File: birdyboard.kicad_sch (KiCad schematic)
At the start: 5 parts, among them U3 TMC2208_SILENTSTEPSTICK, U5 Pico

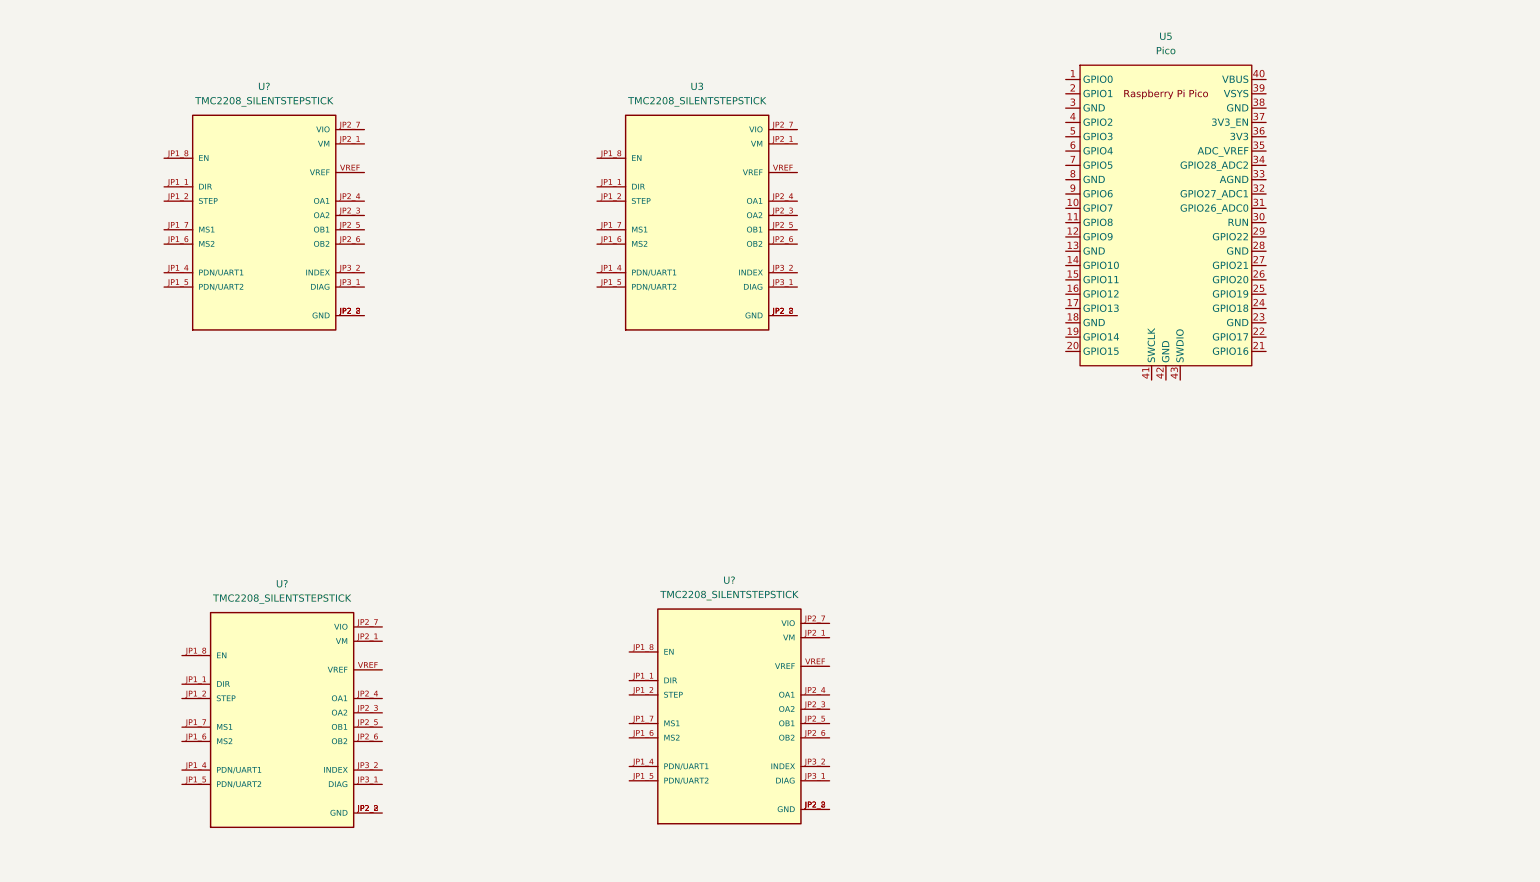
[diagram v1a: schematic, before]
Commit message: Adds the main POWER terminals, adds a symbol and net names for AS5047 board header
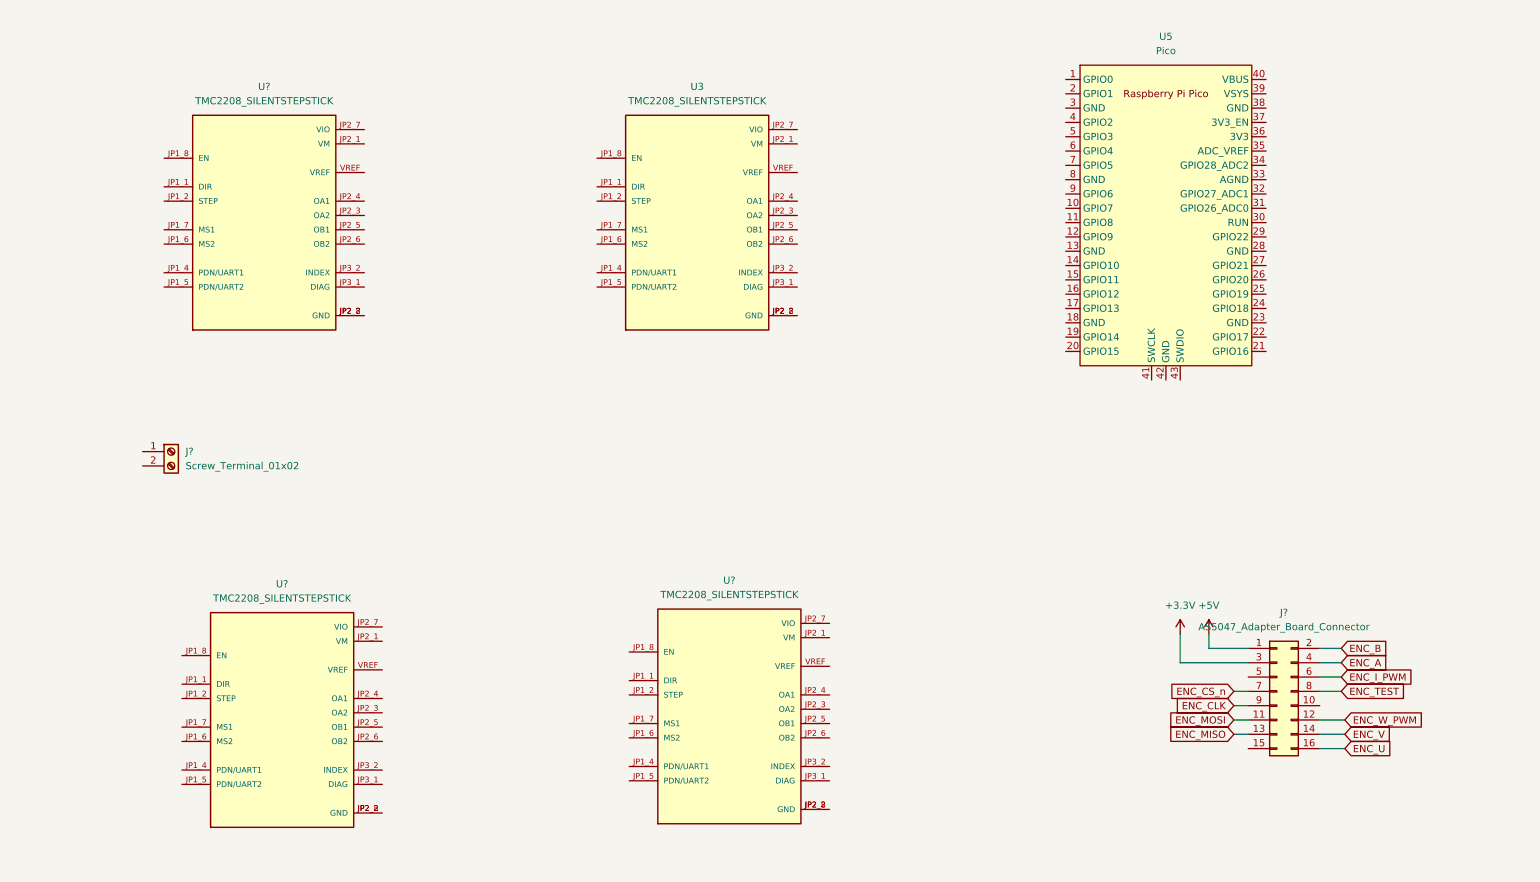
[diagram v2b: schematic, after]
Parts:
- added J?: Screw_Terminal_01x02, birdyboard:CUI_TBP01R2-508-02BE, symbol Connector:Screw_Terminal_01x02
- added J?: AS5047_Adapter_Board_Connector, symbol Connector_Generic:Conn_02x08_Odd_Even
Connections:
- new net +3V3: J?.3 (Pin_3)
- new net +5V: J?.1 (Pin_1)
- new net ENC_A: J?.4 (Pin_4)
- new net ENC_B: J?.2 (Pin_2)
- new net ENC_CLK: J?.9 (Pin_9)
- new net ENC_CS_n: J?.7 (Pin_7)
- new net ENC_I_PWM: J?.6 (Pin_6)
- new net ENC_MISO: J?.13 (Pin_13)
- new net ENC_MOSI: J?.11 (Pin_11)
- new net ENC_TEST: J?.8 (Pin_8)
- new net ENC_U: J?.16 (Pin_16)
- new net ENC_V: J?.14 (Pin_14)
- new net ENC_W_PWM: J?.12 (Pin_12)
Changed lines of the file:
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@@
 (kicad_sch (version 20211123) (generator eeschema)
   (paper "A4")
+  (wire (pts (xy 249.555 140.97) (xy 253.365 140.97))
+    (stroke (width 0) (type default) (color 0 0 0 0))
+  )
+  (wire (pts (xy 249.555 153.67) (xy 254 153.67))
+    (stroke (width 0) (type default) (color 0 0 0 0))
+  )
+  (wire (pts (xy 249.555 148.59) (xy 254 148.59))
+    (stroke (width 0) (type default) (color 0 0 0 0))
+  )
+  (wire (pts (xy 234.315 146.05) (xy 236.855 146.05))
+    (stroke (width 0) (type default) (color 0 0 0 0))
+  )
+  (wire (pts (xy 249.555 151.13) (xy 254 151.13))
+    (stroke (width 0) (type default) (color 0 0 0 0))
+  )
+  (wire (pts (xy 249.555 143.51) (xy 253.365 143.51))
+    (stroke (width 0) (type default) (color 0 0 0 0))
+  )
+  (wire (pts (xy 249.555 138.43) (xy 253.365 138.43))
+    (stroke (width 0) (type default) (color 0 0 0 0))
+  )
+  (wire (pts (xy 236.855 135.89) (xy 229.87 135.89))
+    (stroke (width 0) (type default) (color 0 0 0 0))
+  )
+  (wire (pts (xy 249.555 135.89) (xy 253.365 135.89))
+    (stroke (width 0) (type default) (color 0 0 0 0))
+  )
+  (wire (pts (xy 234.315 143.51) (xy 236.855 143.51))
+    (stroke (width 0) (type default) (color 0 0 0 0))
+  )
+  (wire (pts (xy 224.79 138.43) (xy 224.79 133.35))
+    (stroke (width 0) (type default) (color 0 0 0 0))
+  )
+  (wire (pts (xy 229.87 135.89) (xy 229.87 133.35))
+    (stroke (width 0) (type default) (color 0 0 0 0))
+  )
+  (wire (pts (xy 234.315 148.59) (xy 236.855 148.59))
+    (stroke (width 0) (type default) (color 0 0 0 0))
+  )
+  (wire (pts (xy 234.315 151.13) (xy 236.855 151.13))
+    (stroke (width 0) (type default) (color 0 0 0 0))
+  )
+  (wire (pts (xy 236.855 138.43) (xy 224.79 138.43))
+    (stroke (width 0) (type default) (color 0 0 0 0))
+  )
+  (global_label "ENC_TEST" (shape input) (at 253.365 143.51 0) (fields_autoplaced)
+    (effects (font (size 1.27 1.27)) (justify left))
+    (property "Intersheet References" "${INTERSHEET_REFS}" (id 0) (at 264.7891 143.4306 0)
+      (effects (font (size 1.27 1.27)) (justify left) hide)
+    )
+  )
+  (global_label "ENC_U" (shape input) (at 254 153.67 0) (fields_autoplaced)
+    (effects (font (size 1.27 1.27)) (justify left))
+    (property "Intersheet References" "${INTERSHEET_REFS}" (id 0) (at 262.4607 153.5906 0)
+      (effects (font (size 1.27 1.27)) (justify left) hide)
+    )
+  )
+  (global_label "ENC_MISO" (shape input) (at 234.315 151.13 180) (fields_autoplaced)
+    (effects (font (size 1.27 1.27)) (justify right))
+    (property "Intersheet References" "${INTERSHEET_REFS}" (id 0) (at 222.5886 151.0506 0)
+      (effects (font (size 1.27 1.27)) (justify right) hide)
+    )
+  )
+  (global_label "ENC_CLK" (shape input) (at 234.315 146.05 180) (fields_autoplaced)
+    (effects (font (size 1.27 1.27)) (justify right))
+    (property "Intersheet References" "${INTERSHEET_REFS}" (id 0) (at 223.6167 145.9706 0)
+      (effects (font (size 1.27 1.27)) (justify right) hide)
+    )
+  )
+  (global_label "ENC_V" (shape input) (at 254 151.13 0) (fields_autoplaced)
+    (effects (font (size 1.27 1.27)) (justify left))
+    (property "Intersheet References" "${INTERSHEET_REFS}" (id 0) (at 262.2188 151.0506 0)
+      (effects (font (size 1.27 1.27)) (justify left) hide)
+    )
+  )
+  (global_label "ENC_A" (shape input) (at 253.365 138.43 0) (fields_autoplaced)
+    (effects (font (size 1.27 1.27)) (justify left))
+    (property "Intersheet References" "${INTERSHEET_REFS}" (id 0) (at 261.5838 138.3506 0)
+      (effects (font (size 1.27 1.27)) (justify left) hide)
+    )
+  )
+  (global_label "ENC_CS_n" (shape input) (at 234.315 143.51 180) (fields_autoplaced)
+    (effects (font (size 1.27 1.27)) (justify right))
+    (property "Intersheet References" "${INTERSHEET_REFS}" (id 0) (at 222.5886 143.4306 0)
+      (effects (font (size 1.27 1.27)) (justify right) hide)
+    )
+  )
+  (global_label "ENC_MOSI" (shape input) (at 234.315 148.59 180) (fields_autoplaced)
+    (effects (font (size 1.27 1.27)) (justify right))
+    (property "Intersheet References" "${INTERSHEET_REFS}" (id 0) (at 222.5886 148.5106 0)
+      (effects (font (size 1.27 1.27)) (justify right) hide)
+    )
+  )
+  (global_label "ENC_I_PWM" (shape input) (at 253.365 140.97 0) (fields_autoplaced)
+    (effects (font (size 1.27 1.27)) (justify left))
+    (property "Intersheet References" "${INTERSHEET_REFS}" (id 0) (at 266.2405 140.8906 0)
+      (effects (font (size 1.27 1.27)) (justify left) hide)
+    )
+  )
+  (global_label "ENC_W_PWM" (shape input) (at 254 148.59 0) (fields_autoplaced)
+    (effects (font (size 1.27 1.27)) (justify left))
+    (property "Intersheet References" "${INTERSHEET_REFS}" (id 0) (at 267.7221 148.5106 0)
+      (effects (font (size 1.27 1.27)) (justify left) hide)
+    )
+  )
+  (global_label "ENC_B" (shape input) (at 253.365 135.89 0) (fields_autoplaced)
+    (effects (font (size 1.27 1.27)) (justify left))
+    (property "Intersheet References" "${INTERSHEET_REFS}" (id 0) (at 261.7652 135.8106 0)
+      (effects (font (size 1.27 1.27)) (justify left) hide)
+    )
+  )
   (symbol (lib_id "birdyboard_library:TMC2208_SILENTSTEPSTICK") (at 139.065 59.055 0) (unit 1)
     (in_bom yes) (on_board yes) (fields_autoplaced)
@@
     (pin "VREF")
   )
+  (symbol (lib_id "Connector:Screw_Terminal_01x02") (at 45.72 100.965 0) (unit 1)
+    (in_bom yes) (on_board yes) (fields_autoplaced)
+    (property "Reference" "J?" (id 0) (at 48.26 100.9649 0)
+      (effects (font (size 1.27 1.27)) (justify left))
+    )
+    (property "Value" "Screw_Terminal_01x02" (id 1) (at 48.26 103.5049 0)
+      (effects (font (size 1.27 1.27)) (justify left))
+    )
+    (property "Footprint" "birdyboard:CUI_TBP01R2-508-02BE" (id 2) (at 45.72 100.965 0)
+      (effects (font (size 1.27 1.27)) hide)
+    )
+    (property "Datasheet" "~" (id 3) (at 45.72 100.965 0)
+      (effects (font (size 1.27 1.27)) hide)
+    )
+    (pin "1")
+    (pin "2")
+  )
   (symbol (lib_id "birdyboard_library:TMC2208_SILENTSTEPSTICK") (at 65.405 147.32 0) (unit 1)
     (in_bom yes) (on_board yes) (fields_autoplaced)
@@
     (pin "JP3_2")
     (pin "VREF")
+  )
+  (symbol (lib_id "Connector_Generic:Conn_02x08_Odd_Even") (at 241.935 143.51 0) (unit 1)
+    (in_bom yes) (on_board yes) (fields_autoplaced)
+    (property "Reference" "J?" (id 0) (at 243.205 129.54 0))
+    (property "Value" "AS5047_Adapter_Board_Connector" (id 1) (at 243.205 132.08 0))
+    (property "Footprint" "" (id 2) (at 241.935 143.51 0)
+      (effects (font (size 1.27 1.27)) hide)
+    )
+    (property "Datasheet" "~" (id 3) (at 241.935 143.51 0)
+      (effects (font (size 1.27 1.27)) hide)
+    )
+    (pin "1")
+    (pin "10")
+    (pin "11")
+    (pin "12")
+    (pin "13")
+    (pin "14")
+    (pin "15")
+    (pin "16")
+    (pin "2")
+    (pin "3")
+    (pin "4")
+    (pin "5")
+    (pin "6")
+    (pin "7")
+    (pin "8")
+    (pin "9")
   )
   (symbol (lib_id "birdyboard_library:Pico") (at 222.25 59.055 0) (unit 1)
@@
     (pin "VREF")
   )
+  (symbol (lib_id "power:+5V") (at 229.87 133.35 0) (unit 1)
+    (in_bom yes) (on_board yes) (fields_autoplaced)
+    (property "Reference" "#PWR?" (id 0) (at 229.87 137.16 0)
+      (effects (font (size 1.27 1.27)) hide)
+    )
+    (property "Value" "+5V" (id 1) (at 229.87 128.27 0))
+    (property "Footprint" "" (id 2) (at 229.87 133.35 0)
+      (effects (font (size 1.27 1.27)) hide)
+    )
+    (property "Datasheet" "" (id 3) (at 229.87 133.35 0)
+      (effects (font (size 1.27 1.27)) hide)
+    )
+    (pin "1")
+  )
   (symbol (lib_id "birdyboard_library:TMC2208_SILENTSTEPSTICK") (at 144.78 146.685 0) (unit 1)
     (in_bom yes) (on_board yes) (fields_autoplaced)
@@
     (pin "VREF")
   )
+  (symbol (lib_id "power:+3.3V") (at 224.79 133.35 0) (unit 1)
+    (in_bom yes) (on_board yes) (fields_autoplaced)
+    (property "Reference" "#PWR?" (id 0) (at 224.79 137.16 0)
+      (effects (font (size 1.27 1.27)) hide)
+    )
+    (property "Value" "+3.3V" (id 1) (at 224.79 128.27 0))
+    (property "Footprint" "" (id 2) (at 224.79 133.35 0)
+      (effects (font (size 1.27 1.27)) hide)
+    )
+    (property "Datasheet" "" (id 3) (at 224.79 133.35 0)
+      (effects (font (size 1.27 1.27)) hide)
+    )
+    (pin "1")
+  )
   (sheet_instances
     (path "/" (page "1"))
   )
   (symbol_instances
+    (path "/d0754a39-0cf1-4bbe-83a4-6155f2cbc878"
+      (reference "#PWR?") (unit 1) (value "+5V") (footprint "")
+    )
+    (path "/f76bafbd-6dd5-45ba-8a74-aeca1dbc8b97"
+      (reference "#PWR?") (unit 1) (value "+3.3V") (footprint "")
+    )
+    (path "/1d257dac-277d-4b80-9286-dd0e04ef5f8d"
+      (reference "J?") (unit 1) (value "Screw_Terminal_01x02") (footprint "birdyboard:CUI_TBP01R2-508-02BE")
+    )
+    (path "/3bced514-7c6a-4929-a2f4-97c9dfd34def"
+      (reference "J?") (unit 1) (value "AS5047_Adapter_Board_Connector") (footprint "")
+    )
     (path "/1b7241dd-50c0-4ea4-b9e4-398fecb92930"
       (reference "U3") (unit 1) (value "TMC2208_SILENTSTEPSTICK") (footprint "birdyboard:TMC2208_SILENTSTEPSTICK")

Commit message: update schematic with new connections
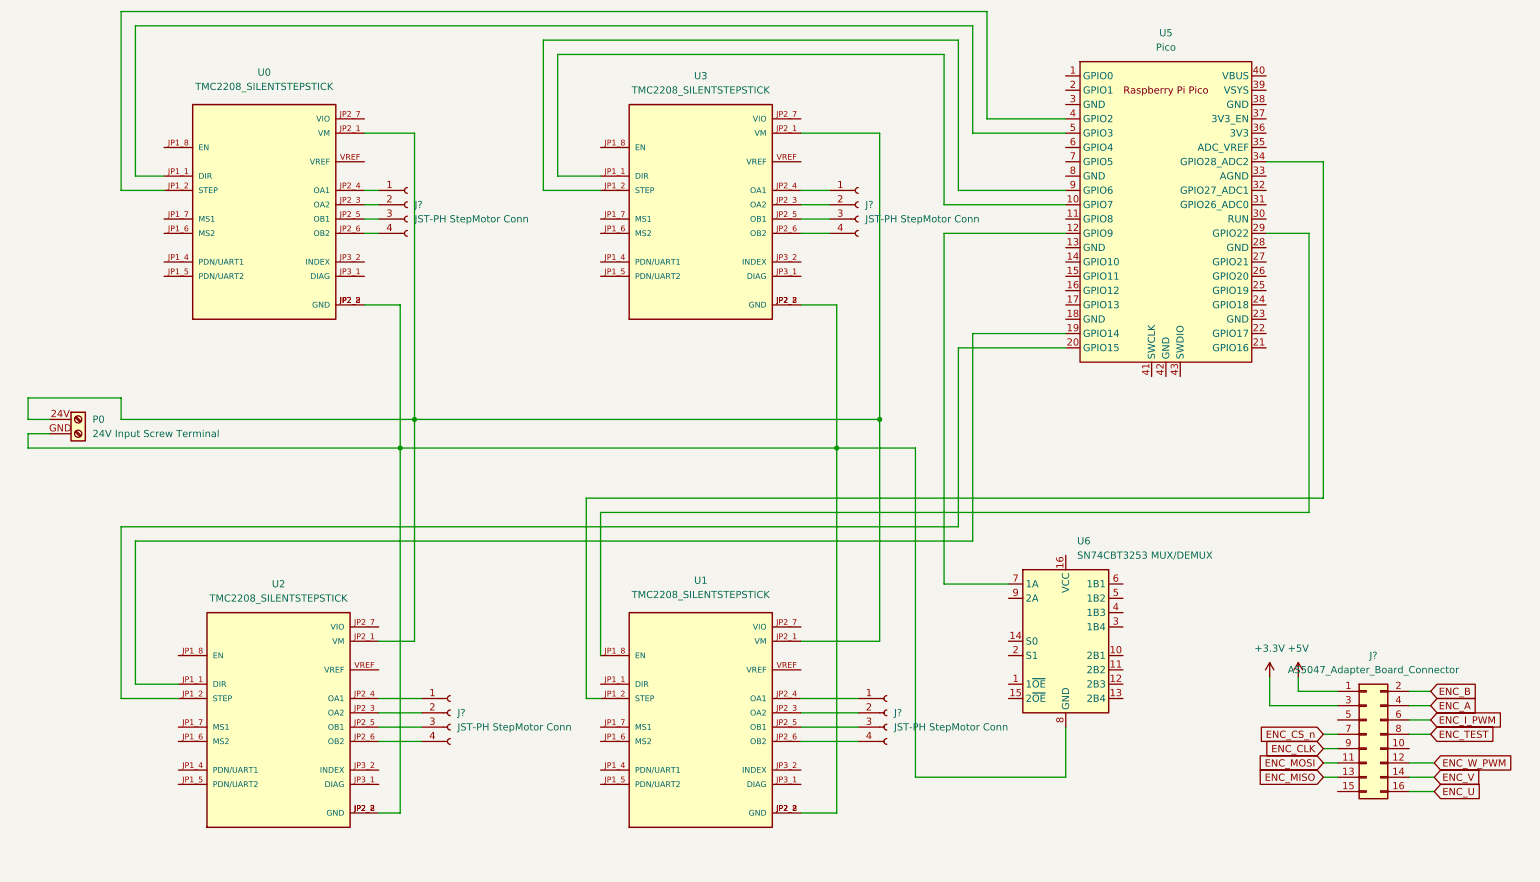
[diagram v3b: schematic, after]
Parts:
- added J? (x4): JST-PH StepMotor Conn, symbol Connector:Conn_01x04_Female
- added U6: SN74CBT3253 MUX/DEMUX, symbol Analog_Switch:SN74CBT3253
- P0: renamed from J?; value Screw_Terminal_01x02 -> 24V Input Screw Terminal
- gave numbers to parts that had none: 3
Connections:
- net at U3.JP1_1 (DIR): now also U5.10 (GPIO7)
- net at U3.JP1_2 (STEP): now also U5.9 (GPIO6)
- net at U3.JP2_1 (VM): now also P0.24V (Pin_1), U0.JP2_1 (VM), U1.JP2_1 (VM), U2.JP2_1 (VM)
- net at U3.JP2_2 (GND), U3.JP2_8 (GND): now also P0.GND (Pin_2), U0.JP2_2 (GND), U0.JP2_8 (GND), U1.JP2_2 (GND), U1.JP2_8 (GND), U2.JP2_2 (GND), U2.JP2_8 (GND), U6.8 (GND)
- net at U3.JP2_3 (OA2): now also J?.2 (Pin_2)
- net at U3.JP2_4 (OA1): now also J?.1 (Pin_1)
- net at U3.JP2_5 (OB1): now also J?.3 (Pin_3)
- net at U3.JP2_6 (OB2): now also J?.4 (Pin_4)
- net at U2.JP1_1 (DIR): now also U5.19 (GPIO14)
- net at U2.JP1_2 (STEP): now also U5.20 (GPIO15)
- net at U2.JP2_3 (OA2): now also J?.2 (Pin_2)
- net at U2.JP2_4 (OA1): now also J?.1 (Pin_1)
- net at U2.JP2_5 (OB1): now also J?.3 (Pin_3)
- net at U2.JP2_6 (OB2): now also J?.4 (Pin_4)
- net at U5.12 (GPIO9): now also U6.7 (1A)
- net at U5.29 (GPIO22): now also U1.JP1_8 (EN)
- net at U5.34 (GPIO28_ADC2): now also U1.JP1_2 (STEP)
- net at U5.4 (GPIO2): now also U0.JP1_2 (STEP)
- net at U5.5 (GPIO3): now also U0.JP1_1 (DIR)
- net at U0.JP2_3 (OA2): now also J?.2 (Pin_2)
- net at U0.JP2_4 (OA1): now also J?.1 (Pin_1)
- net at U0.JP2_5 (OB1): now also J?.3 (Pin_3)
- net at U0.JP2_6 (OB2): now also J?.4 (Pin_4)
- net at U1.JP2_3 (OA2): now also J?.2 (Pin_2)
- net at U1.JP2_4 (OA1): now also J?.1 (Pin_1)
- net at U1.JP2_5 (OB1): now also J?.3 (Pin_3)
- net at U1.JP2_6 (OB2): now also J?.4 (Pin_4)
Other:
- moved on the sheet: J?, P0, U0, U1, U2, U3, U5
